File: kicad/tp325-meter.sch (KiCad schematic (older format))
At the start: 0 parts

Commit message: 7seg display symbol
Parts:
- added R1, R10, R11, R12, R13, R14, R15, R16, R17, R18, R19, R2, R20, R21, R22, R23, R24, R25, R26, R27, R28, R29, R3, R4, R5, R7, R8, R9: 390, symbol tp325-meter:Resistor
- added R6: 470, symbol tp325-meter:Resistor
- added U1, U2, U3, U4: SA56-21SRWA, symbol tp325-meter:SA56-21SRWA
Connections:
- net labels added: +5V, GND
- wire segments 0 -> 97
- no-connect marks 0 -> 3

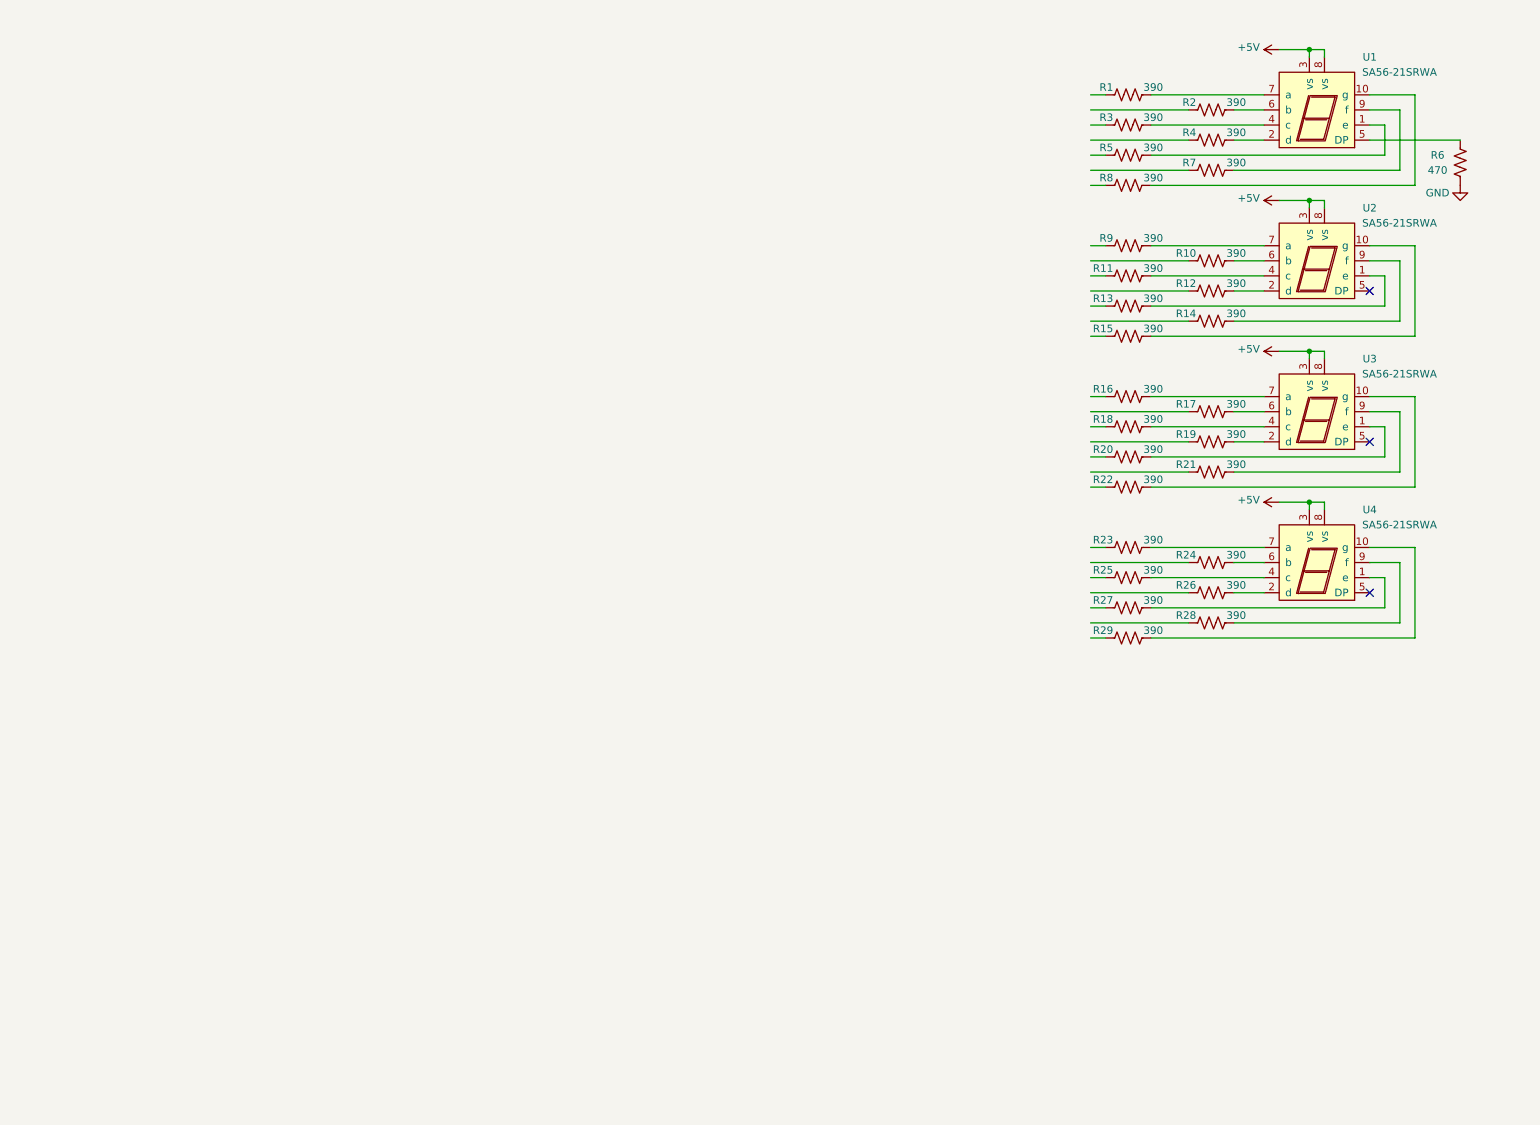
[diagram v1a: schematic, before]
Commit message: add shift registers
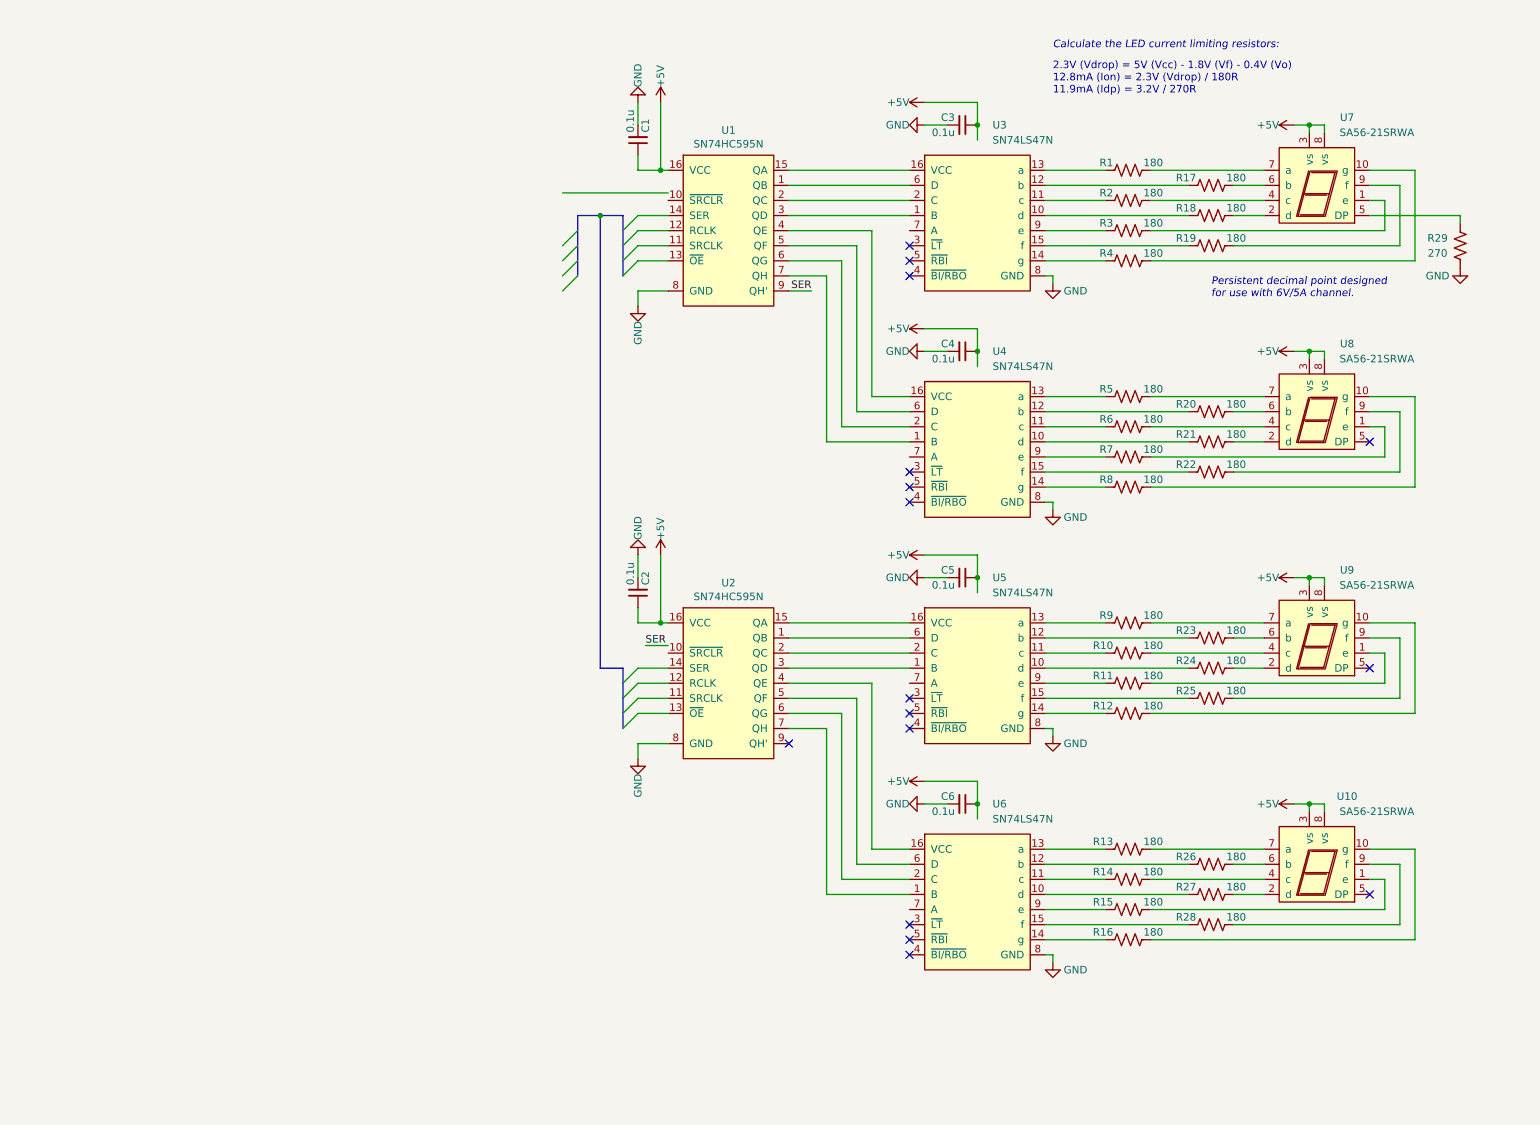
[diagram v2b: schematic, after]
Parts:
- removed R17, R18, R19, R29: 390, symbol tp325-meter:Resistor
- removed U2, U3, U4: SA56-21SRWA, symbol tp325-meter:SA56-21SRWA
- added C1, C2, C3, C4, C5, C6: 0.1u, symbol tp325-meter:Capacitor-Nonpolar
- added R5, R6, R7, R8: 180, symbol tp325-meter:Resistor
- added U1, U2: SN74HC595N, symbol tp325-meter:SN74HC595N
- added U10, U8, U9: SA56-21SRWA, symbol tp325-meter:SA56-21SRWA
- added U3, U4, U5, U6: SN74LS47N, symbol tp325-meter:SN74LS47N
- R1, R10, R11, R12, R13, R14, R15, R16, R20, R21, R22, R23, R24, R25, R26, R27, R28, R9: value 390 -> 180
- R17: renamed from R2; value 390 -> 180
- R18: renamed from R4; value 390 -> 180
- R19: renamed from R7; value 390 -> 180
- R2: renamed from R3; value 390 -> 180
- R29: renamed from R6; value 470 -> 270
- R3: renamed from R5; value 390 -> 180
- R4: renamed from R8; value 390 -> 180
- renumbered U1 to U7
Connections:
- net labels added: SER
- wire segments 97 -> 179
- no-connect marks 3 -> 16
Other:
- note added: "2.3V (Vdrop) = 5V (Vcc) - 1.8V (Vf) - 0.4V (Vo)\n12.8mA (Ion) = 2.3V (Vdrop) / 180R\n11.9mA (Idp) = 3.2V / 270R"
- note added: "Calculate the LED current limiting resistors:"
- note added: "Persistent decimal point designed\nfor use with 6V/5A channel."
- moved on the sheet: R1, R17, R18, R19, R2, R29, R3, R4, U7

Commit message: add microcontroller
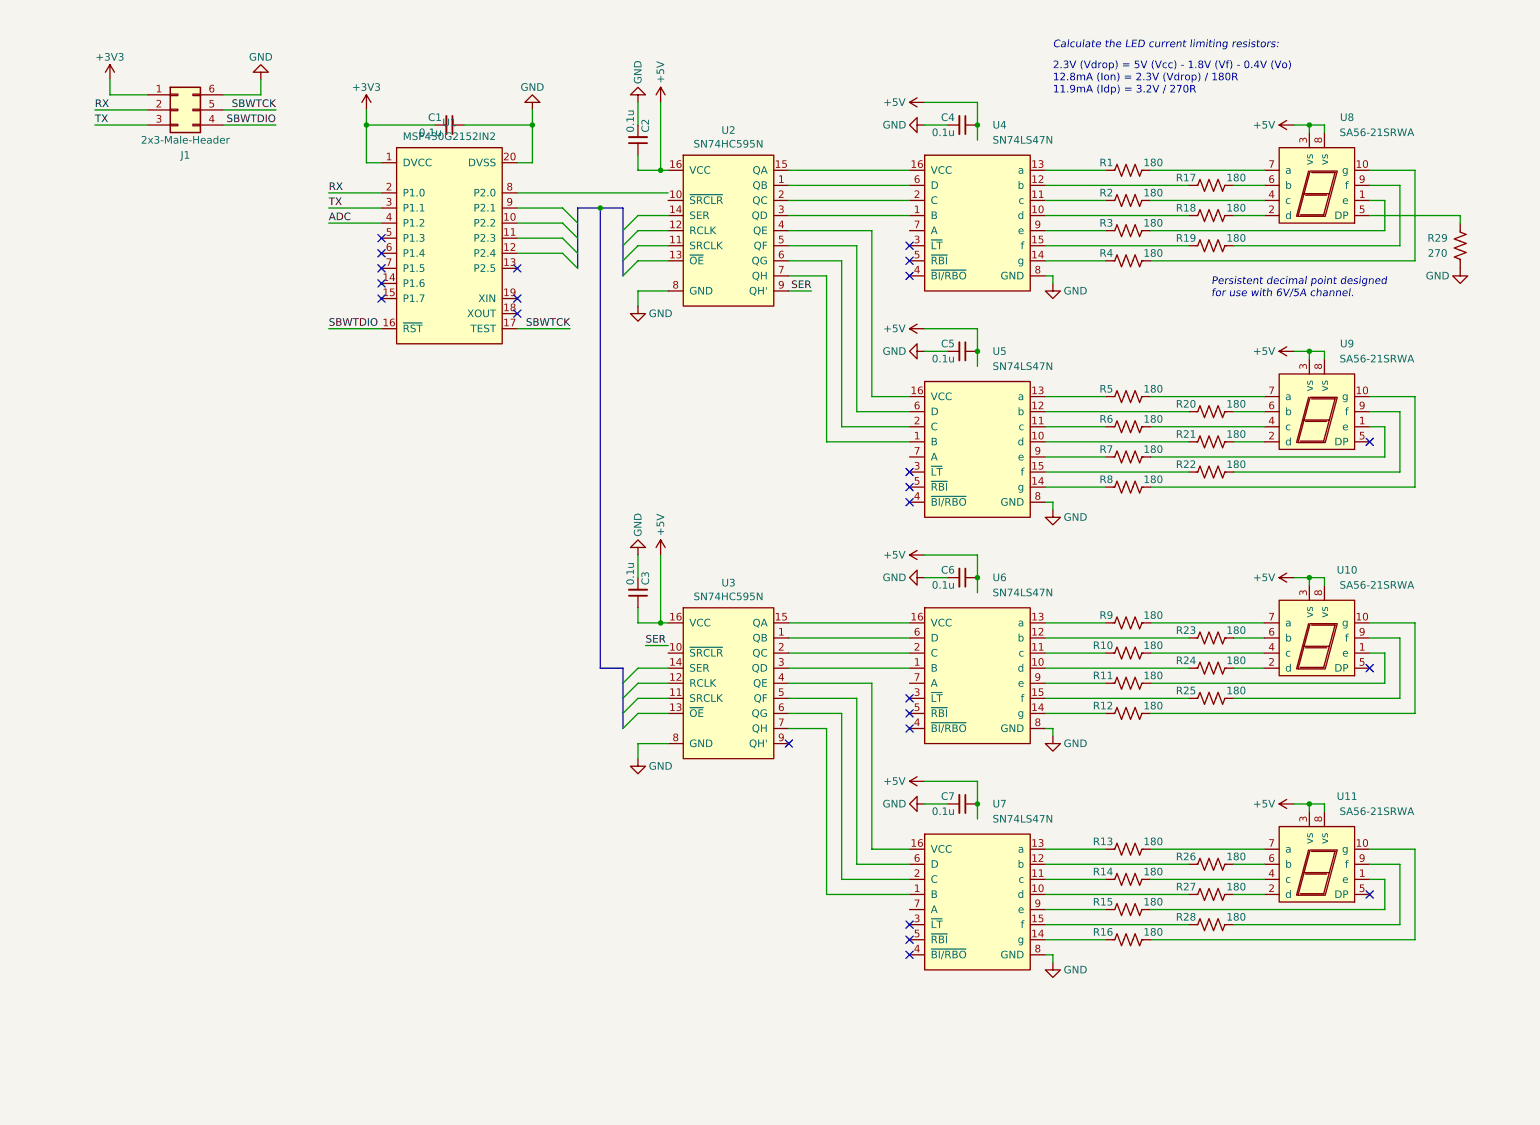
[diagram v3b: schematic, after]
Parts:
- added C1: 0.1u, symbol tp325-meter:Capacitor-Nonpolar
- added J1: 2x3-Male-Header, symbol tp325-meter:2x3-Male-Header
- added U1: MSP430G2152IN2, symbol tp325-meter:MSP430G2152IN2
- renumbered C1 to C2, C2 to C3, C3 to C4, C4 to C5, C5 to C6, C6 to C7, U9 to U10, U10 to U11, U1 to U2, U2 to U3, U3 to U4, U4 to U5, U5 to U6, U6 to U7, U7 to U8, U8 to U9
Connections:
- net labels added: +3V3, ADC, RX, SBWTCK, SBWTDIO, TX
- wire segments 179 -> 204
- no-connect marks 16 -> 24

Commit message: add opamps
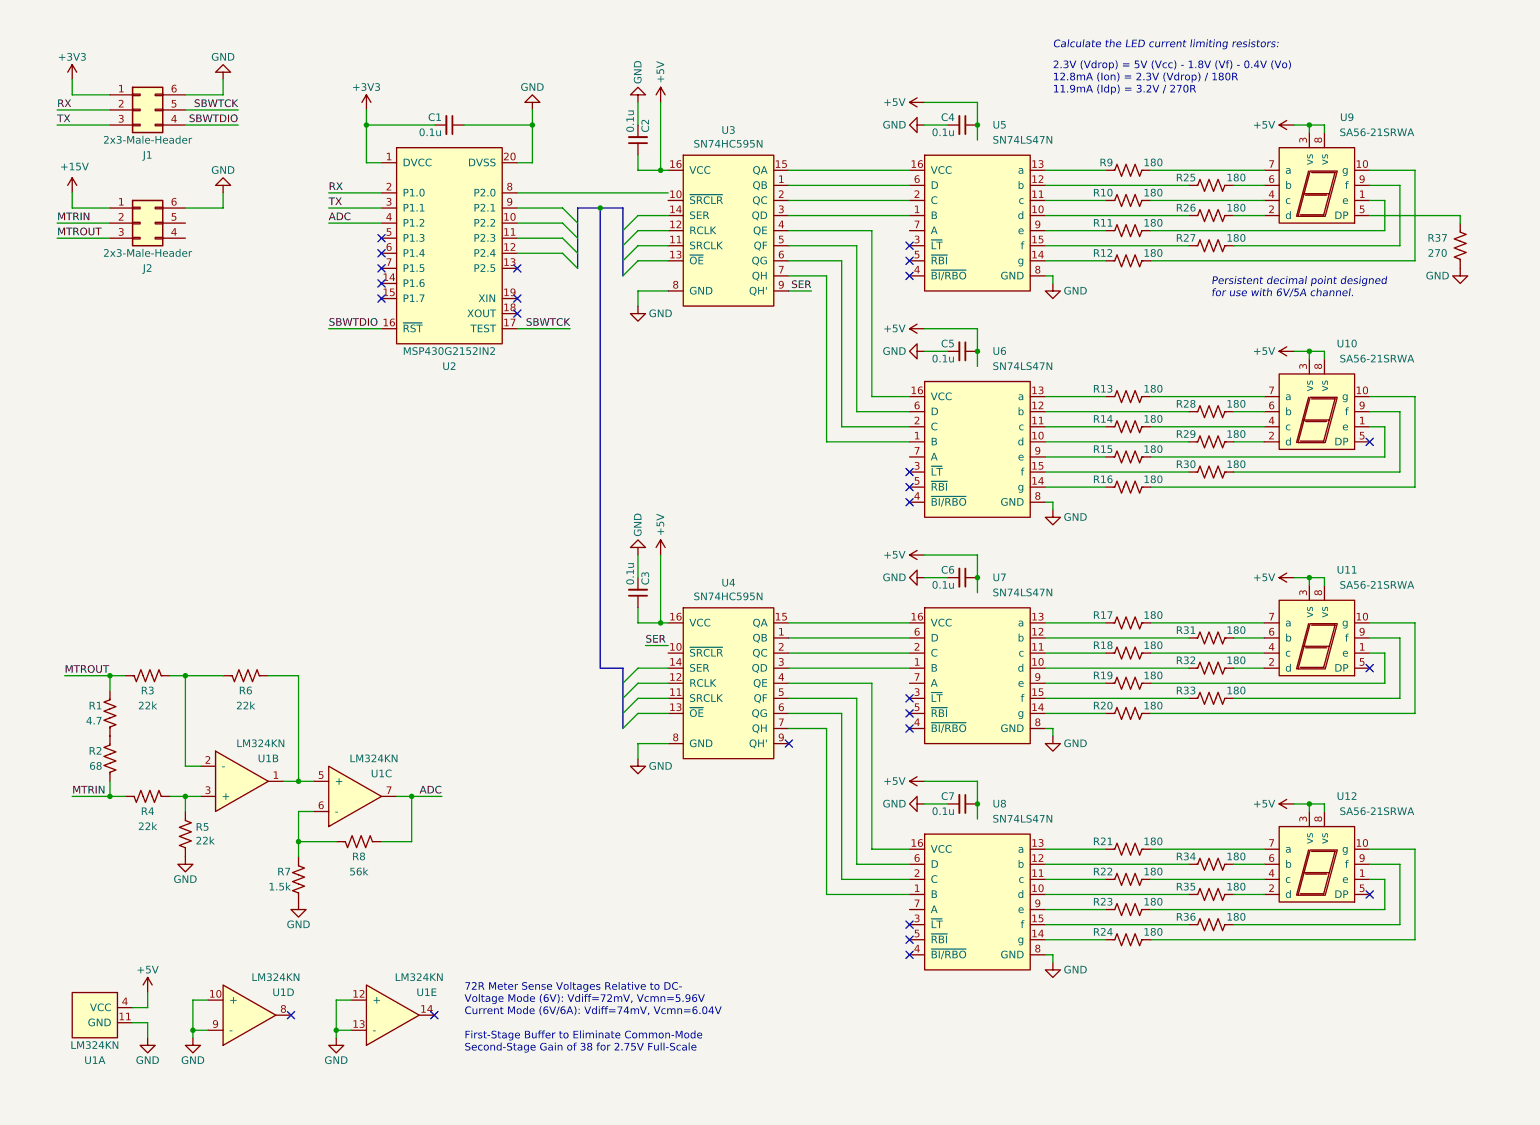
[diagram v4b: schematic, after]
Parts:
- added J2: 2x3-Male-Header, symbol tp325-meter:2x3-Male-Header
- added R1: 4.7, symbol tp325-meter:Resistor
- added R2: 68, symbol tp325-meter:Resistor
- added R3, R4, R5, R6: 22k, symbol tp325-meter:Resistor
- added R7: 1.5k, symbol tp325-meter:Resistor
- added R8: 56k, symbol tp325-meter:Resistor
- added U1: LM324KN, symbol tp325-meter:LM324KN
- renumbered R2 to R10, R3 to R11, R4 to R12, R5 to R13, R6 to R14, R7 to R15, R8 to R16, R9 to R17, R10 to R18, R11 to R19, R12 to R20, R13 to R21, R14 to R22, R15 to R23, R16 to R24, R17 to R25, R18 to R26, R19 to R27, R20 to R28, R21 to R29, R22 to R30, R23 to R31, R24 to R32, R25 to R33, R26 to R34, R27 to R35, R28 to R36, R29 to R37, R1 to R9, U9 to U10, U10 to U11, U11 to U12, U1 to U2, U2 to U3, U3 to U4, U4 to U5, U5 to U6, U6 to U7, U7 to U8, U8 to U9
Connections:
- net +5V: now also U1.4 (VCC)
- net ADC: now also R8.1, U1.7
- net GND: now also J2.6 (Pin_6), R5.2, R7.2, U1.10 (+), U1.11 (GND), U1.12 (+), U1.13 (-), U1.9 (-)
- new net: R6.1, U1.1, U1.5 (+)
- new net: R3.1, R6.2, U1.2 (-)
- new net: R4.1, R5.1, U1.3 (+)
- new net: R7.1, R8.2, U1.6 (-)
- new net: R1.1, R2.2
- new net +15V: J2.1 (Pin_1)
- new net MTRIN: J2.2 (Pin_2), R2.1, R4.2
- new net MTROUT: J2.3 (Pin_3), R1.2, R3.2
- no-connect marks 24 -> 26
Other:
- note added: "72R Meter Sense Voltages Relative to DC-\nVoltage Mode (6V): Vdiff=72mV, Vcmn=5.96V\nCurrent Mode (6V/6A): Vdiff=74mV, Vcmn=6.04V\n\nFirst-Stage Buffer to Eliminate Common-Mode\nSecond-Stage Gain of 38 for 2.75V Full-Scale"
- moved on the sheet: J1

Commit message: add LDOs, pass DRC
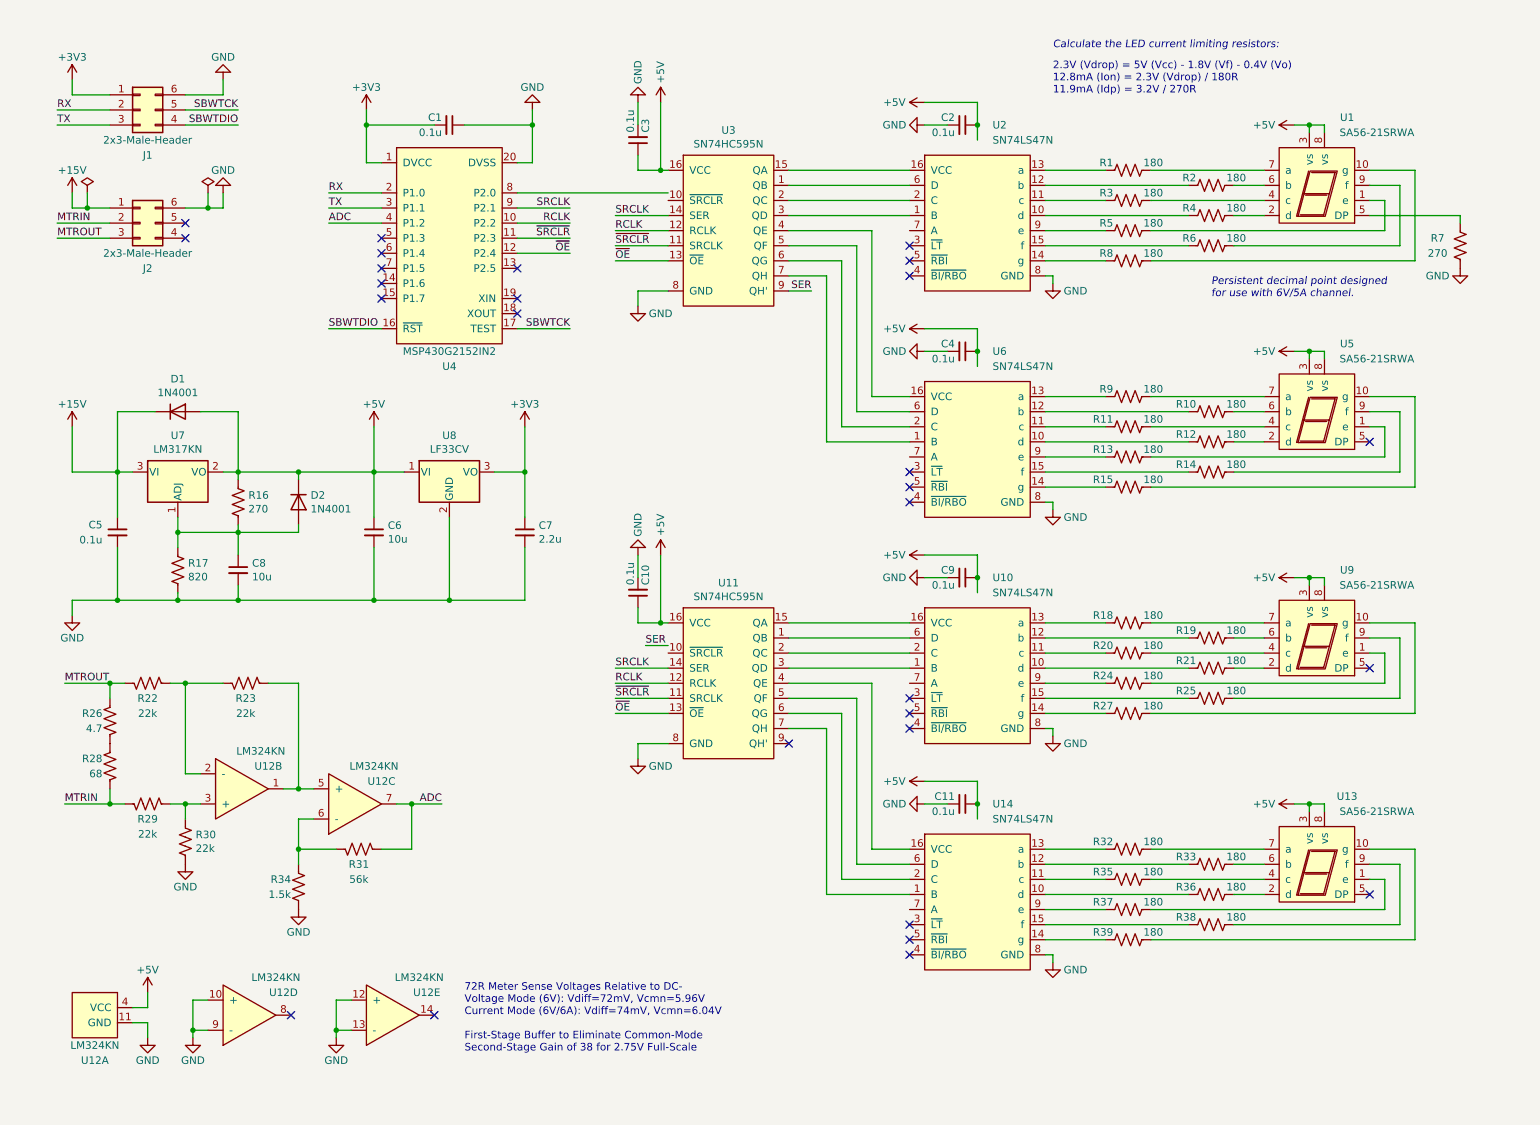
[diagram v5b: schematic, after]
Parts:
- added C5: 0.1u, symbol tp325-meter:Capacitor-Nonpolar
- added C6, C8: 10u, symbol tp325-meter:Capacitor-Nonpolar
- added C7: 2.2u, symbol tp325-meter:Capacitor-Nonpolar
- added D1, D2: 1N4001, symbol tp325-meter:Diode
- added R16: 270, symbol tp325-meter:Resistor
- added R17: 820, symbol tp325-meter:Resistor
- added U7: LM317KN, symbol tp325-meter:LM317KN
- added U8: LF33CV, symbol tp325-meter:LF33CV
- renumbered C3 to C10, C7 to C11, C4 to C2, C2 to C3, C5 to C4, C6 to C9, R9 to R1, R28 to R10, R14 to R11, R29 to R12, R15 to R13, R30 to R14, R16 to R15, R17 to R18, R31 to R19, R25 to R2, R18 to R20, R32 to R21, R3 to R22, R6 to R23, R19 to R24, R33 to R25, R1 to R26, R20 to R27, R2 to R28, R4 to R29, R10 to R3, R5 to R30, R8 to R31, R21 to R32, R34 to R33, R7 to R34, R22 to R35, R35 to R36, R23 to R37, R36 to R38, R24 to R39, R26 to R4, R11 to R5, R27 to R6, R37 to R7, R12 to R8, R13 to R9, U9 to U1, U7 to U10, U4 to U11, U1 to U12, U12 to U13, U8 to U14, U5 to U2, U2 to U4, U10 to U5, U11 to U9
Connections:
- net +15V: now also C5.1, D1.1 (K), U7.3 (VI)
- net +3V3: now also C7.1, U8.3 (VO)
- net +5V: now also C6.1, D1.2 (A), D2.1 (K), R16.1, U7.2 (VO), U8.1 (VI)
- net GND: now also C5.2, C6.2, C7.2, C8.2, R17.2, U8.2 (GND)
- net ~SRCLR: now reaches U3.11 (SRCLK)
- net ~SRCLR: now also U11.11 (SRCLK), U4.11 (P2.3)
- net RCLK: now reaches U3.12 (RCLK)
- net RCLK: now also U11.12 (RCLK), U4.10 (P2.2)
- net ~OE: now reaches U3.13 (~OE)
- net ~OE: now also U11.13 (~OE), U4.12 (P2.4)
- net SRCLK: now reaches U3.14 (SER)
- net SRCLK: now also U11.14 (SER), U4.9 (P2.1)
- new net: C8.1, D2.2 (A), R16.2, R17.1, U7.1 (ADJ)
- no-connect marks 26 -> 28
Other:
- moved on the sheet: R22, R23, R26, R28, R29, R30, R31, R34, U12B, U12C
